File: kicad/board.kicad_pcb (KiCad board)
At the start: 2 copper layers, 155.7 x 107.9 mm, 58 parts

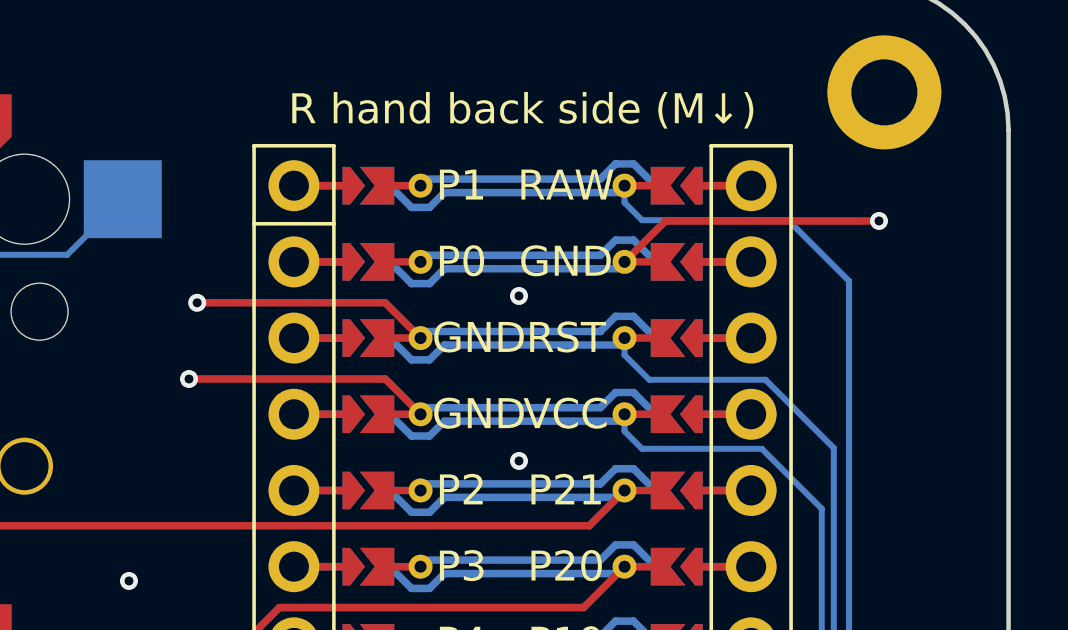
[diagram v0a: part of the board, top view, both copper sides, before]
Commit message: things to consider:
- add inline fuse for battery
- lots of vias in the ground planes
- don't bother doing ground traces
- get the design rules off JLPCP and then put them in kicad
- make the main power trace a bit wider (3 mm)
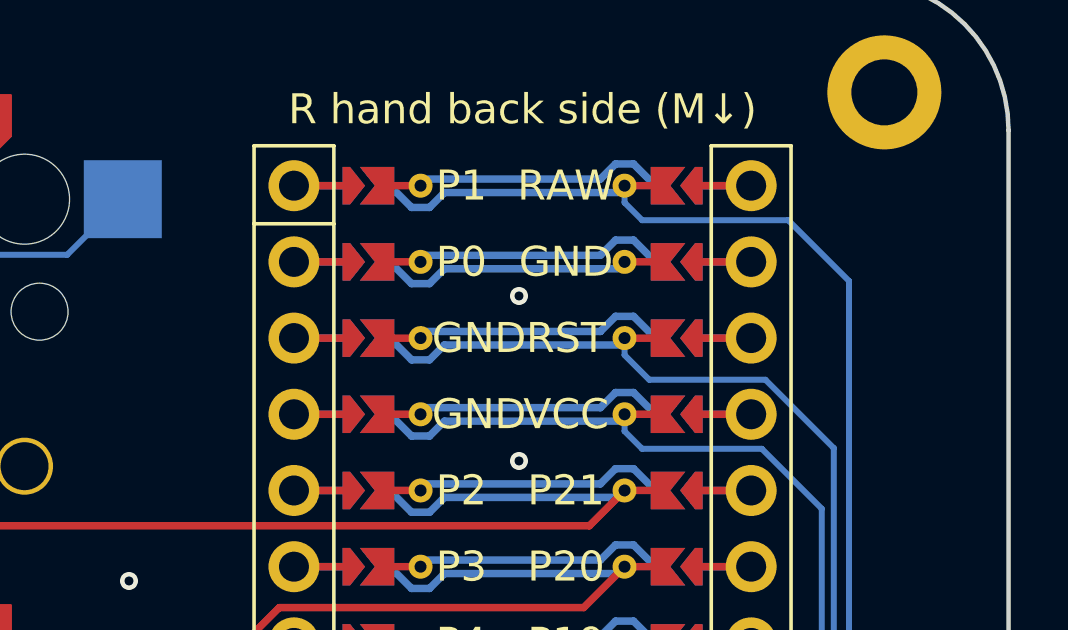
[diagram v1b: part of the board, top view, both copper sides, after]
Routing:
- net GND: track 54.7 -> 29.5 mm, vias 29 -> 26
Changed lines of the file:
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@@
-	)
-	(segment
-		(start 271.381981 84.5)
-		(end 278.5 84.5)
-		(width 0.25)
-		(layer "F.Cu")
-		(net 3)
-	)
-	(segment
-		(start 255.772471 87.227529)
-		(end 262.042452 87.227529)
-		(width 0.25)
-		(layer "F.Cu")
-		(net 3)
-	)
-	(segment
-		(start 255.5 89.767529)
-		(end 262.042452 89.767529)
-		(width 0.25)
-		(layer "F.Cu")
-		(net 3)
-	)
-	(segment
-		(start 262.042452 89.767529)
-		(end 263.218452 90.943529)
-		(width 0.25)
-		(layer "F.Cu")
-		(net 3)
-	)
-	(segment
-		(start 262.042452 87.227529)
-		(end 263.218452 88.403529)
-		(width 0.25)
-		(layer "F.Cu")
-		(net 3)
 	)
 	(segment
@@
 		(width 0.25)
 		(layer "F.Cu")
-		(net 3)
-	)
-	(segment
-		(start 270.018452 85.863529)
-		(end 271.381981 84.5)
-		(width 0.25)
-		(layer "F.Cu")
-		(net 3)
-	)
-	(via
-		(at 278.5 84.5)
-		(size 0.6)
-		(drill 0.3)
-		(layers "F.Cu" "B.Cu")
 		(net 3)
 	)
@@
 		(layers "F.Cu" "B.Cu")
 		(free yes)
-		(net 3)
-	)
-	(via
-		(at 255.772471 87.227529)
-		(size 0.6)
-		(drill 0.3)
-		(layers "F.Cu" "B.Cu")
 		(net 3)
 	)
@@
 		(net 3)
 	)
-	(via
-		(at 255.5 89.767529)
-		(size 0.6)
-		(drill 0.3)
-		(layers "F.Cu" "B.Cu")
-		(net 3)
-	)

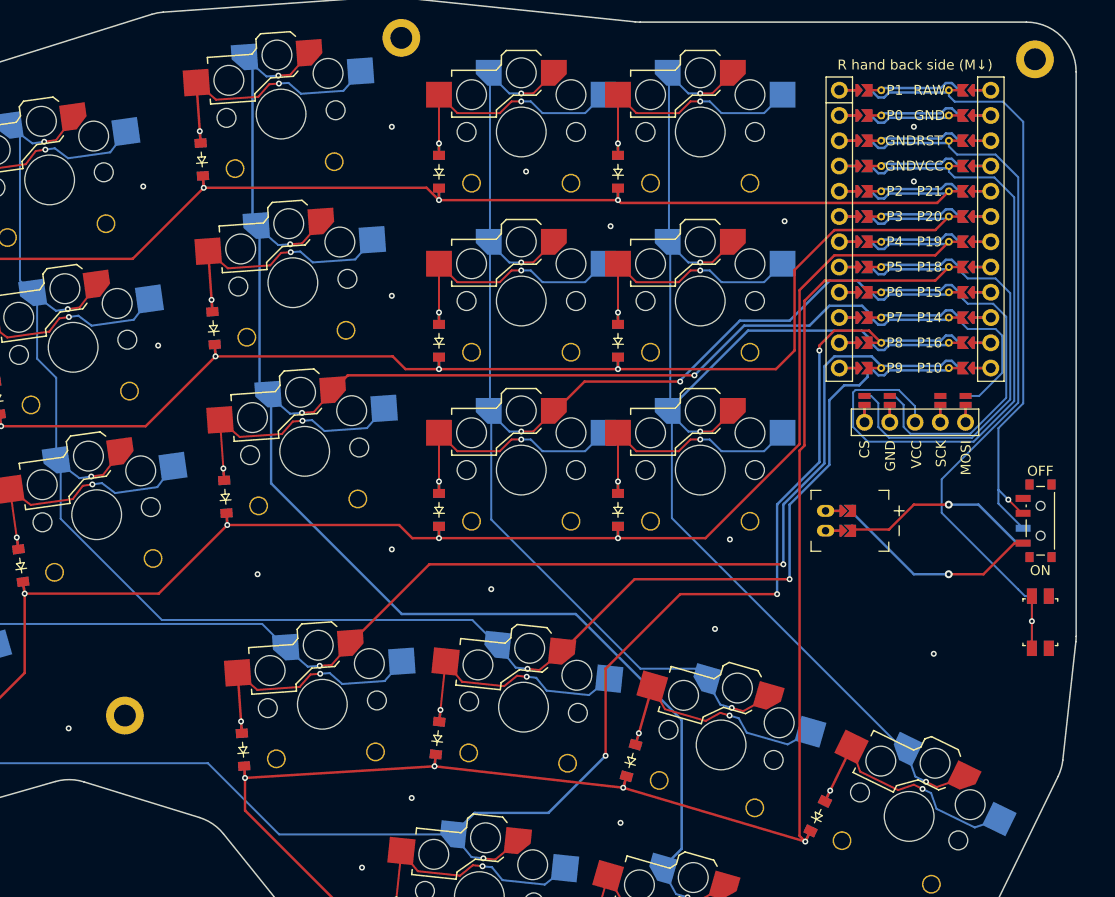
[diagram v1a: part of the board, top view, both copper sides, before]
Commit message: improving routing
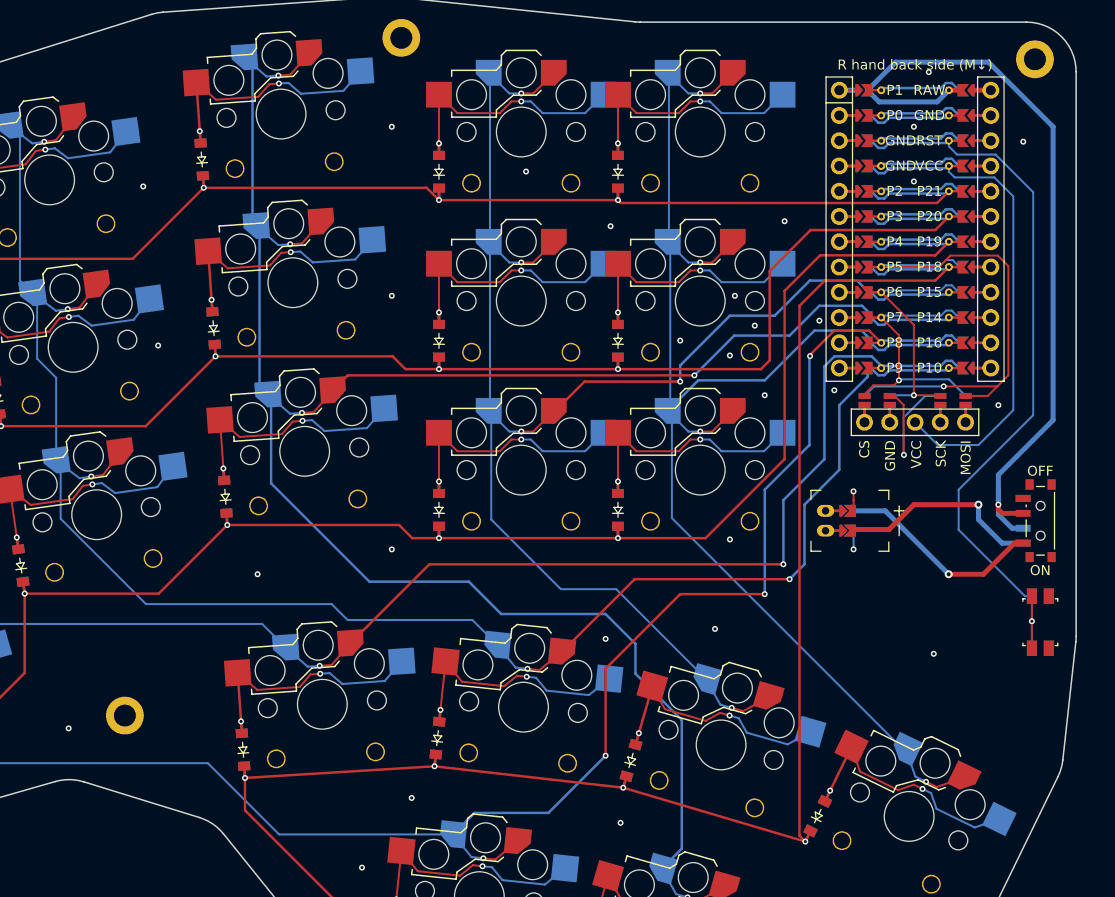
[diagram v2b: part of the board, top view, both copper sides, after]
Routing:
- net GND: track 29.5 -> 48.5 mm, vias 26 -> 39
- net VCC: track 69.1 -> 51.7 mm
- net RAW: track 65.4 -> 81.5 mm
- net SCK: track 39.9 -> 27.2 mm, vias 0 -> 1
- net MOSI: track 46.2 -> 53.7 mm, vias 0 -> 1
- net CS: track 23.3 -> 28.8 mm, vias 0 -> 1
- net P14: track 211.9 -> 213.7 mm
- net P15: track 154.0 -> 154.9 mm
- net P10: track 185.0 -> 184.1 mm
- net P19: track 188.8 -> 189.6 mm
- net P8: track 248.1 -> 247.4 mm
- net BAT_P: track 40.9 -> 41.6 mm
- net P20: track 182.6 -> 183.1 mm
- net MCU1_24: track 4.24 -> 3.74 mm

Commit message: minor
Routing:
- net BAT_P: track 41.6 -> 40.7 mm
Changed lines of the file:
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@@
 	)
 	(segment
-		(start 260.557981 127.5)
-		(end 260.434452 127.623529)
+		(start 271.5 125)
+		(end 266.5 125)
+		(width 0.5)
+		(layer "F.Cu")
+		(net 75)
+	)
+	(segment
+		(start 264 127.5)
+		(end 260.557981 127.5)
 		(width 0.5)
 		(layer "F.Cu")
@@
 	)
 	(segment
-		(start 273 125)
-		(end 266.5 125)
-		(width 0.5)
-		(layer "F.Cu")
-		(net 75)
-	)
-	(segment
-		(start 264 127.5)
-		(end 260.557981 127.5)
+		(start 273 126.5)
+		(end 271.5 125)
 		(width 0.5)
 		(layer "F.Cu")
@@
 		(net 75)
 	)
+	(segment
+		(start 260.557981 127.5)
+		(end 260.434452 127.623529)
+		(width 0.5)
+		(layer "F.Cu")
+		(net 75)
+	)
 	(via
 		(at 270 132)
@@
 	)
 	(via
-		(at 273 125)
+		(at 273 126.5)
 		(size 0.8)
 		(drill 0.4)
@@
 		(width 0.5)
 		(layer "B.Cu")
-		(net 75)
-	)
-	(segment
-		(start 273 125)
-		(end 273 126.5)
-		(width 0.5)
-		(layer "B.Cu")
